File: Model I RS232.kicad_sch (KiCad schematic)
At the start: 28 parts, among them U1 HD6402, U10 74LS08, U2 COM8116, U3 74LS155, U4 74LS04, U5 74LS00, U6 74LS244, U7 74LS367, U8 74LS174, U9 SP3243ECA-L/TR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

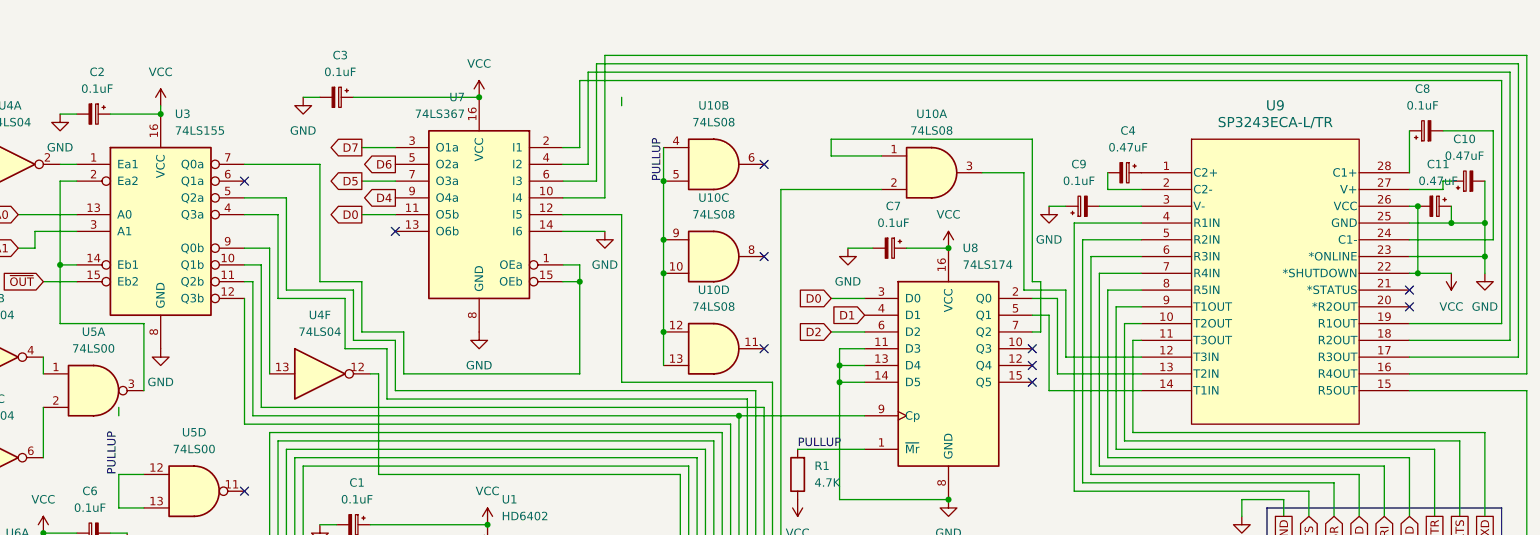
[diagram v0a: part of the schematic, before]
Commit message: Add files via upload
Update schematic and PCB to version 1.1 -- 05 April 2025

1. change PCB footprint to eliminate mechanical interference with mounting post
2. modify footprint of J1 pads to fit more closely
3. fix schematic error causing U9 to be in permanent shutdown mode
4. Clean up some very ugly routing
5. Change version information on silkscreen
6. embed silkscreen logo as footprint to fix missing font error
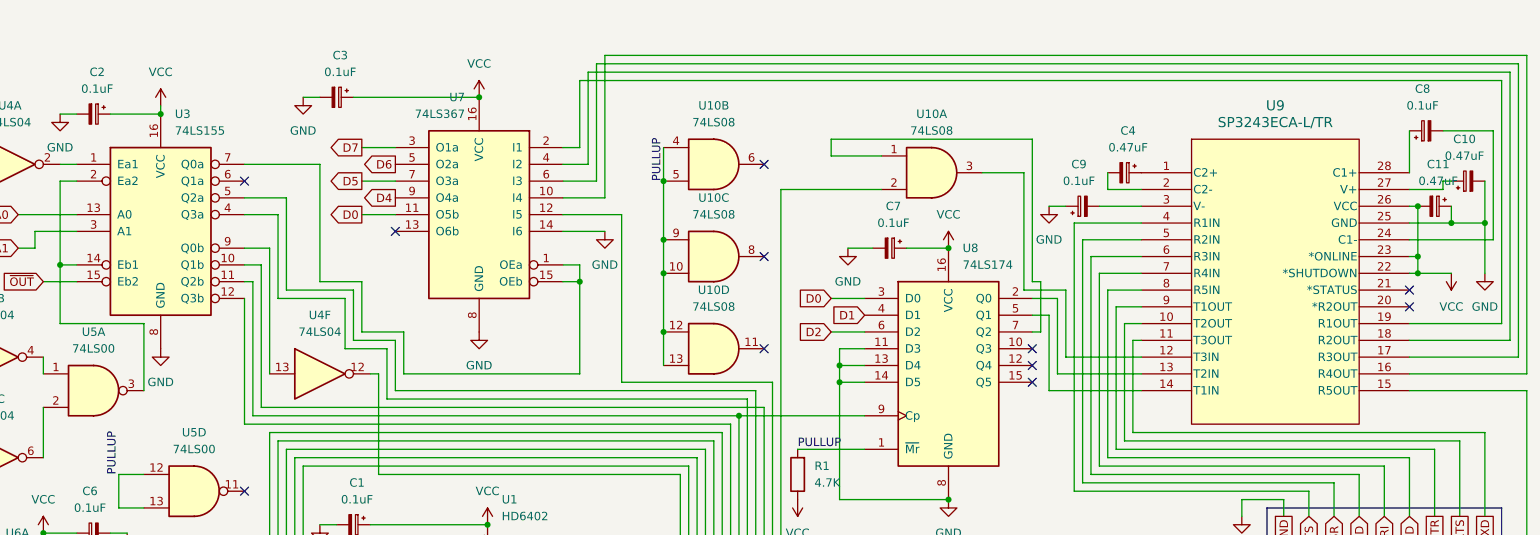
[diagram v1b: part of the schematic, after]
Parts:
- J1: now left out of the parts list
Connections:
- net GND: no longer U9.23 (*ONLINE)
- net VCC: now also U9.23 (*ONLINE)
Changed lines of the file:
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@@
 	(title_block
 		(title "TRS-80 Model I RS-232 Interface")
+		(date "2025-04-05")
+		(rev "1.1")
 		(company "Roger Murley/BYTESHiFT")
 	)
@@
 	)
 	(junction
-		(at 276.86 44.45)
-		(diameter 0)
-		(color 0 0 0 0)
-	)
-	(junction
 		(at 280.67 124.46)
 		(diameter 0)
@@
 	)
 	(junction
+		(at 266.7 44.45)
+		(diameter 0)
+		(color 0 0 0 0)
+	)
+	(junction
 		(at 96.52 105.41)
 		(diameter 0)
@@
 	(wire
 		(pts
-			(xy 266.7 36.83) (xy 266.7 46.99)
-		)
-		(stroke
-			(width 0)
-			(type default)
-		)
-	)
-	(wire
-		(pts
-			(xy 265.43 44.45) (xy 276.86 44.45)
+			(xy 266.7 36.83) (xy 266.7 44.45)
 		)
 		(stroke
@@
 	(wire
 		(pts
-			(xy 69.85 67.31) (xy 69.85 68.58)
-		)
-		(stroke
-			(width 0)
-			(type default)
-		)
-	)
-	(wire
-		(pts
 			(xy 88.9 30.48) (xy 100.33 30.48)
 		)
@@
 	(wire
 		(pts
-			(xy 276.86 46.99) (xy 276.86 44.45)
+			(xy 276.86 39.37) (xy 276.86 46.99)
 		)
 		(stroke
@@
 	(wire
 		(pts
+			(xy 265.43 44.45) (xy 266.7 44.45)
+		)
+		(stroke
+			(width 0)
+			(type default)
+		)
+	)
+	(wire
+		(pts
 			(xy 224.79 64.77) (xy 210.82 64.77)
 		)
@@
 	(wire
 		(pts
-			(xy 146.05 20.32) (xy 146.05 21.59)
-		)
-		(stroke
-			(width 0)
-			(type default)
-		)
-	)
-	(wire
-		(pts
 			(xy 207.01 31.75) (xy 200.66 31.75)
 		)
@@
 	(wire
 		(pts
+			(xy 266.7 44.45) (xy 266.7 46.99)
+		)
+		(stroke
+			(width 0)
+			(type default)
+		)
+	)
+	(wire
+		(pts
 			(xy 88.9 110.49) (xy 88.9 152.4)
 		)
@@
 	(wire
 		(pts
-			(xy 276.86 44.45) (xy 276.86 39.37)
-		)
-		(stroke
-			(width 0)
-			(type default)
-		)
-	)
-	(wire
-		(pts
 			(xy 265.43 39.37) (xy 271.78 39.37)
 		)
@@
 		(unit 1)
 		(exclude_from_sim no)
-		(in_bom yes)
+		(in_bom no)
 		(on_board yes)
 		(dnp no)

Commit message: Add files via upload
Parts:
- added J2: Conn_01x03_Pin, Connector_PinHeader_2.54mm:PinHeader_1x03_P2.54mm_Vertical, symbol Connector:Conn_01x03_Pin
- added J3: Conn_01x04_Pin, Connector_PinHeader_2.54mm:PinHeader_1x04_P2.54mm_Vertical, symbol Connector:Conn_01x04_Pin
- added J4, J5: Conn_01x02_Pin, Connector_PinHeader_2.54mm:PinHeader_1x02_P2.54mm_Vertical, symbol Connector:Conn_01x02_Pin
- C11: value 0.47uF -> 0.1uF
- C15: footprint Capacitor_THT:C_Radial_D6.3mm_H11.0mm_P2.50mm -> Capacitor_SMD:C_0805_2012Metric_Pad1.18x1.45mm_HandSolder
- U3: footprint Package_DIP:DIP-16_W7.62mm_Socket_LongPads -> Package_SO:SOIC-16_3.9x9.9mm_P1.27mm
- U9: footprint Package_SO:TSSOP-28_4.4x9.7mm_P0.65mm -> Package_SO:SSOP-28_5.3x10.2mm_P0.65mm
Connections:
- net GND: now also J2.3 (Pin_3), J3.1 (Pin_1), J3.2 (Pin_2)
- net RXD: now also J5.1 (Pin_1)
- net TXD: now also J5.2 (Pin_2)
- net VCC: now also J2.1 (Pin_1), J3.4 (Pin_4); no longer U9.22 (*SHUTDOWN)
- net at Y1.1: now also U2.18 (XTAL/EXT2); no longer U2.1 (XTAL/EXT1)
- net at Y1.2: now also U2.1 (XTAL/EXT1); no longer U2.18 (XTAL/EXT2)
- net RX_TTL: now reaches U1.20 (RX_SERIAL), U7.12 (I5), U9.15 (R5OUT)
- net RX_TTL: now also J4.2 (Pin_2)
- net TX_TTL: now reaches U10.3, U9.12 (T3IN)
- net TX_TTL: now also J4.1 (Pin_1)
- new net ~{SHUTDOWN}: J2.2 (Pin_2), U9.22 (*SHUTDOWN)
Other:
- moved on the sheet: C1, C15, R1, U1, U4A, U4D, U5B, U5C
